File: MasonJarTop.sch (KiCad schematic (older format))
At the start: 17 parts, among them P1 CONN_01X02, P2 Loop Mounting Hole, P3 Loop Mounting Hole

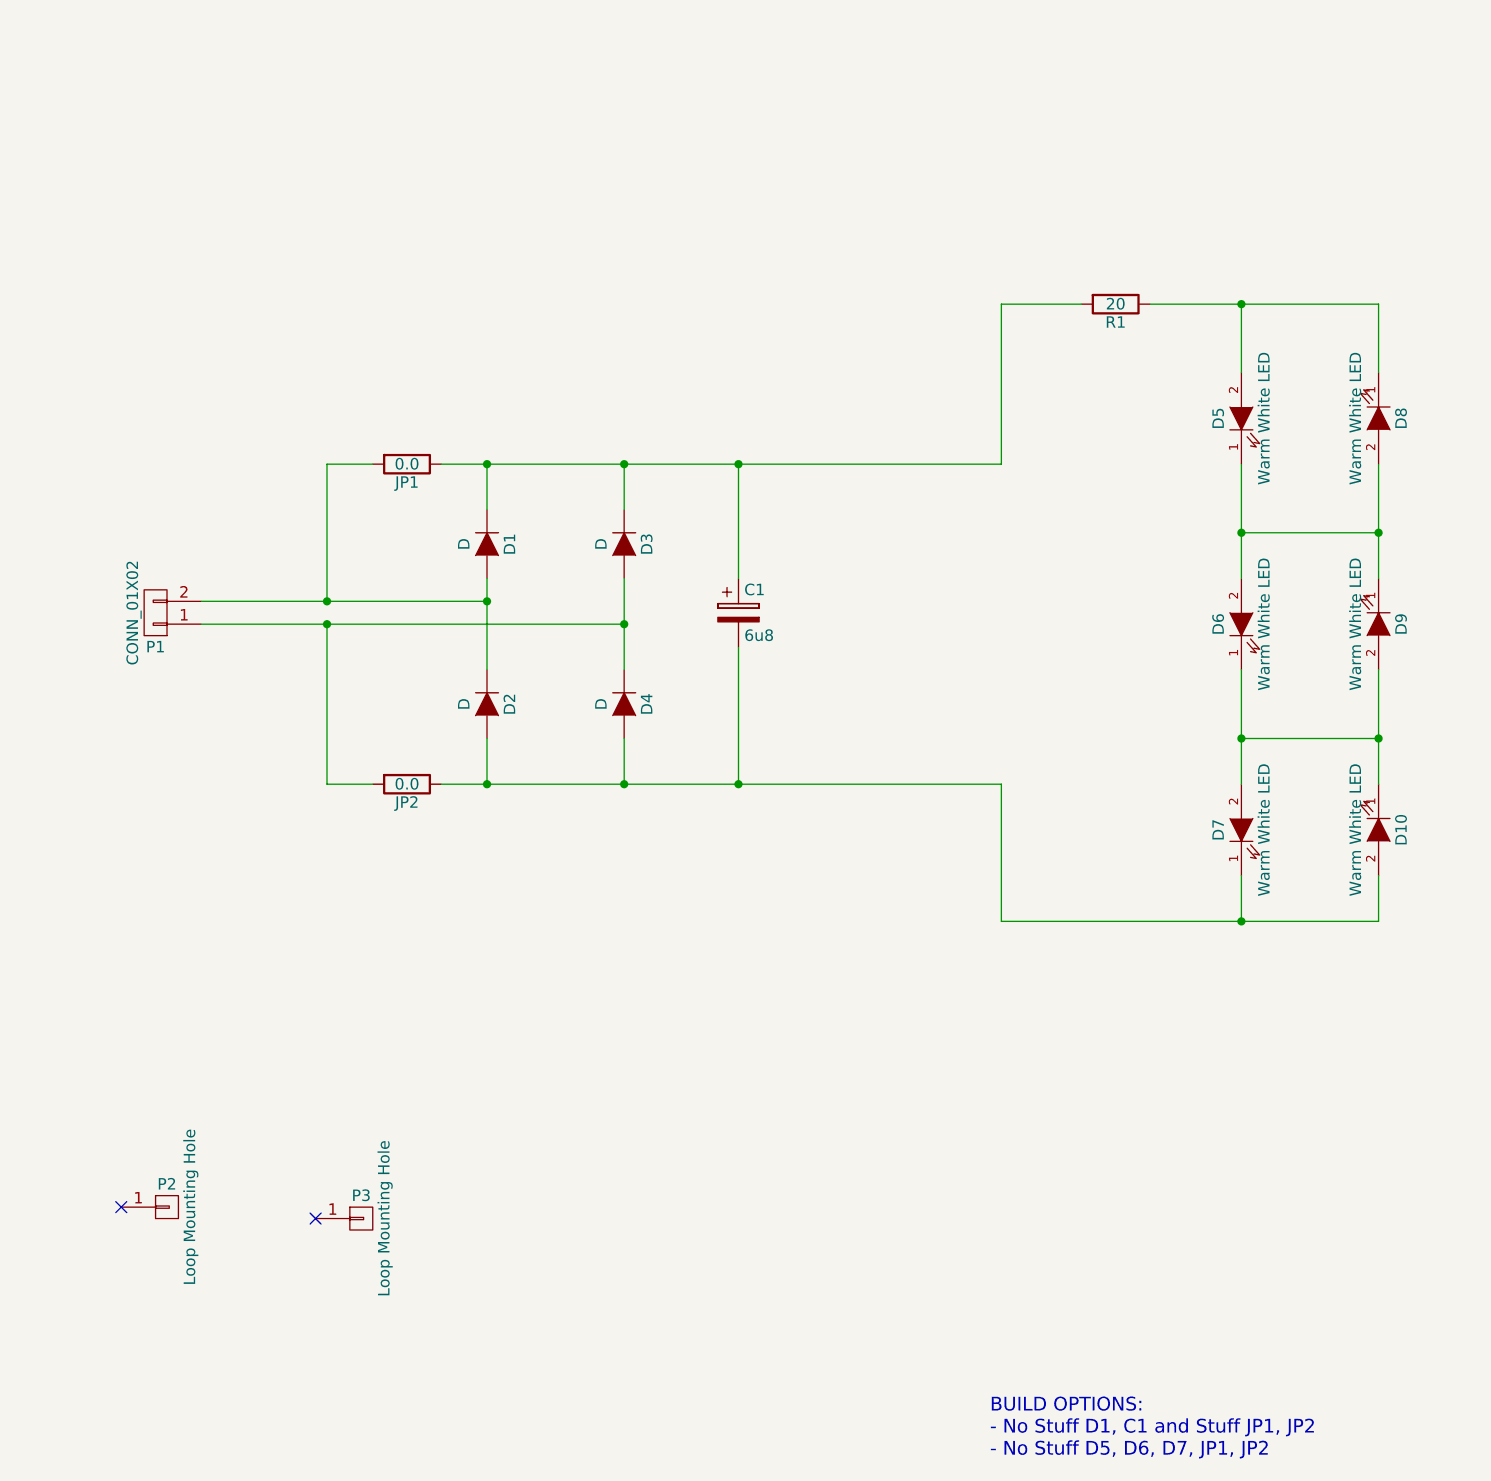
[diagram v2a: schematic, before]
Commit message: Modify schematic after testing and re-layout complete.
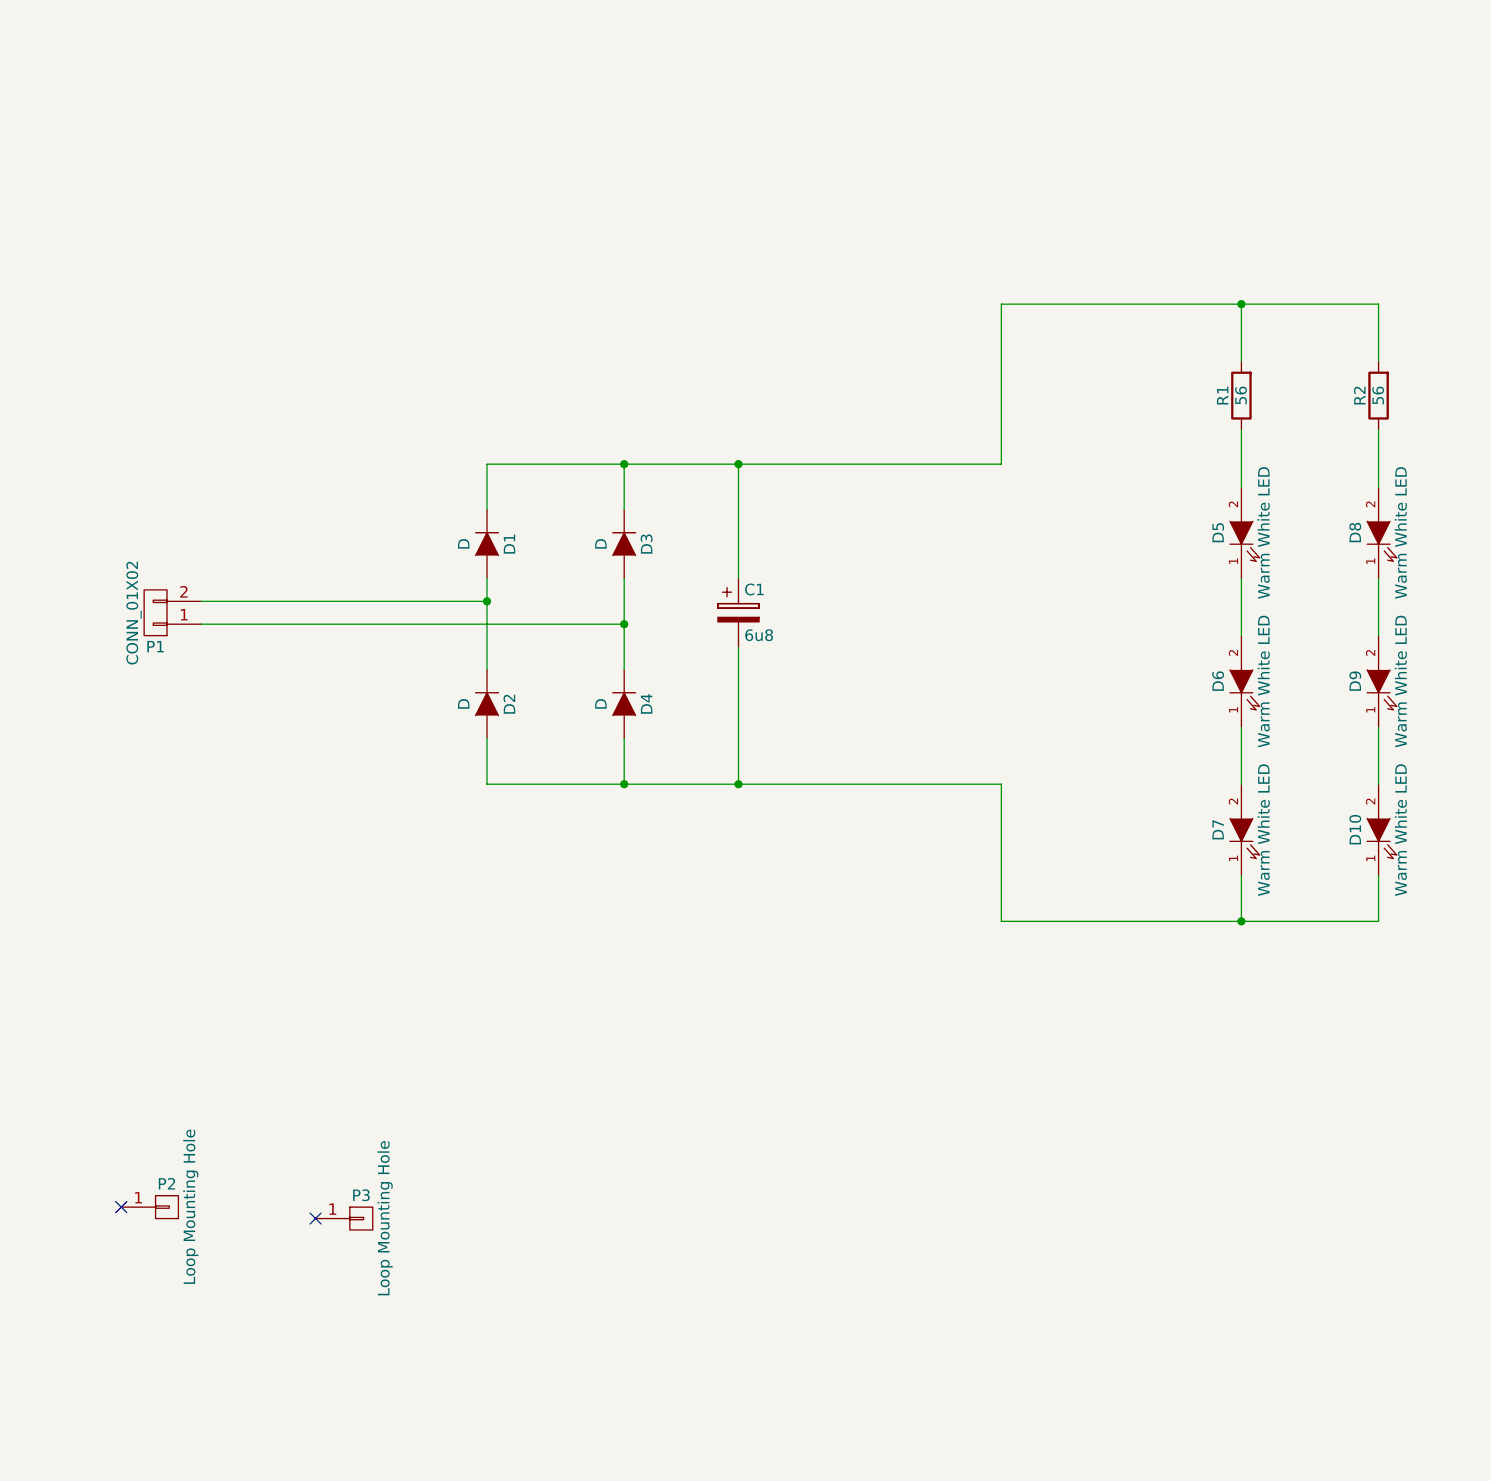
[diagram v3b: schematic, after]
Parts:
- removed JP1, JP2: 0.0, Resistors_SMD:R_1206_HandSoldering, symbol R
- added R2: 56, Resistors_SMD:R_1206_HandSoldering, symbol R
- D1, D2, D3, D4: footprint Diodes_SMD:SOD-123 -> LEDs:LED_1206
- R1: value 20 -> 56; DigiKey 311-20ERCT-ND -> 311-56ERCT-ND
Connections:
- net at D5.1 (K), D6.2 (A): no longer D8.2 (A), D9.1 (K)
- net at D5.2 (A), R1.1: no longer D8.1 (K)
- net at D6.1 (K), D7.2 (A): no longer D10.1 (K), D9.2 (A)
- net at C1.2, D2.2 (A), D4.2 (A)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: now also D10.1 (K); no longer D10.2 (A)
- net at C1.1, D1.1 (K), D3.1 (K)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: now also R2.2
- new net: D8.1 (K), D9.2 (A)
- new net: D8.2 (A), R2.1
- new net: D10.2 (A), D9.1 (K)
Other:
- note removed: "BUILD OPTIONS:\n- No Stuff D1, C1 and Stuff JP1, JP2\n- No Stuff D5, D6, D7, JP1, JP2"
- moved on the sheet: D5, D6, D8, D9, R1
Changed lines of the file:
@@
 encoding utf-8
 Sheet 1 1
-Title ""
-Date ""
-Rev ""
-Comp ""
+Title "Mason Jar Lamp"
+Date "2016-07-06"
+Rev "B"
+Comp "DPW 2016"
 Comment1 ""
 Comment2 ""
@@
 L LED D5
 U 1 1 576C2FA9
-P 7400 2800
-F 0 "D5" H 7400 2900 50  0000 C CNN
-F 1 "Warm White LED" H 7400 2700 50  0000 C CNN
-F 2 "LEDs:LED_1206" H 7400 2800 60  0001 C CNN
-F 3 "" H 7400 2800 60  0000 C CNN
-F 4 "1416-1216-1-ND" H 7400 2800 60  0001 C CNN "DigiKey"
-	1    7400 2800
+P 7400 3300
+F 0 "D5" H 7400 3400 50  0000 C CNN
+F 1 "Warm White LED" H 7400 3200 50  0000 C CNN
+F 2 "LEDs:LED_1206" H 7400 3300 60  0001 C CNN
+F 3 "" H 7400 3300 60  0000 C CNN
+F 4 "1416-1216-1-ND" H 7400 3300 60  0001 C CNN "DigiKey"
+	1    7400 3300
 	0    -1   -1   0
 $EndComp
@@
 L LED D6
 U 1 1 576C3263
-P 7400 3700
-F 0 "D6" H 7400 3800 50  0000 C CNN
-F 1 "Warm White LED" H 7400 3600 50  0000 C CNN
-F 2 "LEDs:LED_1206" H 7400 3700 60  0001 C CNN
-F 3 "" H 7400 3700 60  0000 C CNN
-F 4 "1416-1216-1-ND" H 7400 3700 60  0001 C CNN "DigiKey"
-	1    7400 3700
+P 7400 3950
+F 0 "D6" H 7400 4050 50  0000 C CNN
+F 1 "Warm White LED" H 7400 3850 50  0000 C CNN
+F 2 "LEDs:LED_1206" H 7400 3950 60  0001 C CNN
+F 3 "" H 7400 3950 60  0000 C CNN
+F 4 "1416-1216-1-ND" H 7400 3950 60  0001 C CNN "DigiKey"
+	1    7400 3950
 	0    -1   -1   0
 $EndComp
@@
 L R R1
 U 1 1 576C34CD
-P 6850 2300
-F 0 "R1" V 6930 2300 50  0000 C CNN
-F 1 "20" V 6850 2300 50  0000 C CNN
-F 2 "Resistors_SMD:R_1206_HandSoldering" V 6780 2300 30  0001 C CNN
-F 3 "" H 6850 2300 30  0000 C CNN
-F 4 "311-20ERCT-ND" V 6850 2300 60  0001 C CNN "DigiKey"
-	1    6850 2300
-	0    1    1    0
+P 7400 2700
+F 0 "R1" V 7480 2700 50  0000 C CNN
+F 1 "56" V 7400 2700 50  0000 C CNN
+F 2 "Resistors_SMD:R_1206_HandSoldering" V 7330 2700 30  0001 C CNN
+F 3 "" H 7400 2700 30  0000 C CNN
+F 4 "311-56ERCT-ND" V 7400 2700 60  0001 C CNN "DigiKey"
+	1    7400 2700
+	-1   0    0    1
 $EndComp
 $Comp
@@
 L LED D8
 U 1 1 576D6D77
-P 8000 2800
-F 0 "D8" H 8000 2900 50  0000 C CNN
-F 1 "Warm White LED" H 8000 2700 50  0000 C CNN
-F 2 "LEDs:LED_1206" H 8000 2800 60  0001 C CNN
-F 3 "" H 8000 2800 60  0000 C CNN
-F 4 "1416-1216-1-ND" H 8000 2800 60  0001 C CNN "DigiKey"
-	1    8000 2800
-	0    1    1    0
+P 8000 3300
+F 0 "D8" H 8000 3400 50  0000 C CNN
+F 1 "Warm White LED" H 8000 3200 50  0000 C CNN
+F 2 "LEDs:LED_1206" H 8000 3300 60  0001 C CNN
+F 3 "" H 8000 3300 60  0000 C CNN
+F 4 "1416-1216-1-ND" H 8000 3300 60  0001 C CNN "DigiKey"
+	1    8000 3300
+	0    -1   -1   0
 $EndComp
 $Comp
 L LED D9
 U 1 1 576D6DBF
-P 8000 3700
-F 0 "D9" H 8000 3800 50  0000 C CNN
-F 1 "Warm White LED" H 8000 3600 50  0000 C CNN
-F 2 "LEDs:LED_1206" H 8000 3700 60  0001 C CNN
-F 3 "" H 8000 3700 60  0000 C CNN
-F 4 "1416-1216-1-ND" H 8000 3700 60  0001 C CNN "DigiKey"
-	1    8000 3700
-	0    1    1    0
+P 8000 3950
+F 0 "D9" H 8000 4050 50  0000 C CNN
+F 1 "Warm White LED" H 8000 3850 50  0000 C CNN
+F 2 "LEDs:LED_1206" H 8000 3950 60  0001 C CNN
+F 3 "" H 8000 3950 60  0000 C CNN
+F 4 "1416-1216-1-ND" H 8000 3950 60  0001 C CNN "DigiKey"
+	1    8000 3950
+	0    -1   -1   0
 $EndComp
 $Comp
@@
 F 4 "1416-1216-1-ND" H 8000 4600 60  0001 C CNN "DigiKey"
 	1    8000 4600
-	0    1    1    0
-$EndComp
-Text Notes 6300 7350 0    60   ~ 0
-BUILD OPTIONS:\n- No Stuff D1, C1 and Stuff JP1, JP2\n- No Stuff D5, D6, D7, JP1, JP2
-$Comp
-L R JP1
-U 1 1 576D7B6C
-P 3750 3000
-F 0 "JP1" V 3830 3000 50  0000 C CNN
-F 1 "0.0" V 3750 3000 50  0000 C CNN
-F 2 "Resistors_SMD:R_1206_HandSoldering" V 3680 3000 30  0001 C CNN
-F 3 "" H 3750 3000 30  0000 C CNN
-F 4 "311-20ERCT-ND" V 3750 3000 60  0001 C CNN "DigiKey"
-	1    3750 3000
-	0    1    1    0
-$EndComp
-$Comp
-L R JP2
-U 1 1 576D7BEA
-P 3750 4400
-F 0 "JP2" V 3830 4400 50  0000 C CNN
-F 1 "0.0" V 3750 4400 50  0000 C CNN
-F 2 "Resistors_SMD:R_1206_HandSoldering" V 3680 4400 30  0001 C CNN
-F 3 "" H 3750 4400 30  0000 C CNN
-F 4 "311-20ERCT-ND" V 3750 4400 60  0001 C CNN "DigiKey"
-	1    3750 4400
-	0    1    1    0
+	0    -1   -1   0
 $EndComp
 $Comp
@@
 F 0 "D3" H 4700 3450 50  0000 C CNN
 F 1 "D" H 4700 3250 50  0000 C CNN
-F 2 "Diodes_SMD:SOD-123" H 4700 3350 50  0001 C CNN
+F 2 "LEDs:LED_1206" H 4700 3350 50  0001 C CNN
 F 3 "" H 4700 3350 50  0000 C CNN
 F 4 "DA2JF2300LCT-ND" H 4700 3350 60  0001 C CNN "DigiKey"
@@
 F 0 "D1" H 4100 3450 50  0000 C CNN
 F 1 "D" H 4100 3250 50  0000 C CNN
-F 2 "Diodes_SMD:SOD-123" H 4100 3350 50  0001 C CNN
+F 2 "LEDs:LED_1206" H 4100 3350 50  0001 C CNN
 F 3 "" H 4100 3350 50  0000 C CNN
 F 4 "DA2JF2300LCT-ND" H 4100 3350 60  0001 C CNN "DigiKey"
@@
 F 0 "D2" H 4100 4150 50  0000 C CNN
 F 1 "D" H 4100 3950 50  0000 C CNN
-F 2 "Diodes_SMD:SOD-123" H 4100 4050 50  0001 C CNN
+F 2 "LEDs:LED_1206" H 4100 4050 50  0001 C CNN
 F 3 "" H 4100 4050 50  0000 C CNN
 F 4 "DA2JF2300LCT-ND" H 4100 4050 60  0001 C CNN "DigiKey"
@@
 F 0 "D4" H 4700 4150 50  0000 C CNN
 F 1 "D" H 4700 3950 50  0000 C CNN
-F 2 "Diodes_SMD:SOD-123" H 4700 4050 50  0001 C CNN
+F 2 "LEDs:LED_1206" H 4700 4050 50  0001 C CNN
 F 3 "" H 4700 4050 50  0000 C CNN
 F 4 "DA2JF2300LCT-ND" H 4700 4050 60  0001 C CNN "DigiKey"
@@
 $EndComp
 Wire Wire Line
-	7400 2300 7400 2600
-Wire Wire Line
-	7400 3000 7400 3500
-Wire Wire Line
-	7400 3900 7400 4400
-Wire Wire Line
 	7400 4800 7400 5000
-Wire Wire Line
-	8000 2300 8000 2600
-Wire Wire Line
-	8000 3000 8000 3500
-Wire Wire Line
-	7400 3300 8000 3300
-Connection ~ 8000 3300
-Connection ~ 7400 3300
-Wire Wire Line
-	8000 3900 8000 4400
-Wire Wire Line
-	8000 5000 8000 4800
-Wire Wire Line
-	7400 4200 8000 4200
-Connection ~ 8000 4200
-Connection ~ 7400 4200
 Wire Wire Line
 	4100 3900 4100 3500
@@
 Connection ~ 4100 3600
 Wire Wire Line
-	2850 3700 4700 3700
-Connection ~ 4700 3700
-Wire Wire Line
-	3900 3000 6350 3000
-Wire Wire Line
 	4100 3000 4100 3200
 Wire Wire Line
-	4700 3000 4700 3200
-Connection ~ 4100 3000
-Wire Wire Line
-	3900 4400 6350 4400
-Wire Wire Line
-	4100 4400 4100 4200
+	4100 4400 6350 4400
 Wire Wire Line
 	4700 4400 4700 4200
-Connection ~ 4100 4400
-Wire Wire Line
-	3600 4400 3400 4400
-Wire Wire Line
-	3400 4400 3400 3700
-Connection ~ 3400 3700
-Wire Wire Line
-	3600 3000 3400 3000
-Wire Wire Line
-	3400 3000 3400 3600
-Connection ~ 3400 3600
-Wire Wire Line
-	5200 3000 5200 3500
-Connection ~ 4700 3000
 Wire Wire Line
 	5200 4400 5200 3800
 Connection ~ 4700 4400
-Wire Wire Line
-	7000 2300 8000 2300
-Connection ~ 7400 2300
 Wire Wire Line
 	6350 5000 8000 5000
@@
 	6350 3000 6350 2300
 Wire Wire Line
-	6350 2300 6700 2300
+	6350 2300 8000 2300
+Wire Wire Line
+	4100 3000 6350 3000
+Wire Wire Line
+	5200 3500 5200 3000
 Connection ~ 5200 3000
+Wire Wire Line
+	4700 3200 4700 3000
+Connection ~ 4700 3000
+$Comp
+L R R2
+U 1 1 577DEC45
+P 8000 2700
+F 0 "R2" V 8080 2700 50  0000 C CNN
+F 1 "56" V 8000 2700 50  0000 C CNN
+F 2 "Resistors_SMD:R_1206_HandSoldering" V 7930 2700 30  0001 C CNN
+F 3 "" H 8000 2700 30  0000 C CNN
+F 4 "311-56ERCT-ND" V 8000 2700 60  0001 C CNN "DigiKey"
+	1    8000 2700
+	-1   0    0    1
+$EndComp
+Wire Wire Line
+	8000 5000 8000 4800
+Wire Wire Line
+	8000 4400 8000 4150
+Wire Wire Line
+	8000 3750 8000 3500
+Wire Wire Line
+	7400 4400 7400 4150
+Wire Wire Line
+	7400 3750 7400 3500
+Wire Wire Line
+	7400 3100 7400 2850
+Wire Wire Line
+	8000 3100 8000 2850
+Wire Wire Line
+	8000 2300 8000 2550
+Wire Wire Line
+	7400 2550 7400 2300
+Connection ~ 7400 2300
+Wire Wire Line
+	4100 4200 4100 4400
+Wire Wire Line
+	2850 3700 4700 3700
+Connection ~ 4700 3700
 $EndSCHEMATC
